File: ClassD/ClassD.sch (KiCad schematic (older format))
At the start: 37 parts, among them J1 RCJ-01X, J2 RCJ-01X, P1 CONN_01X02, SW1 FSM2JSMAA, U1 AP1117E50G-13, U2 TPA2008D2

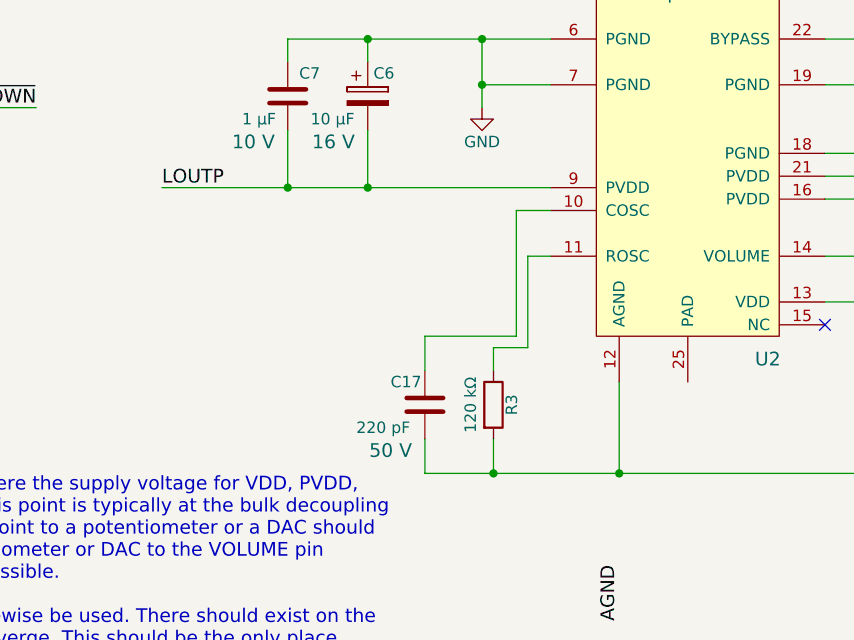
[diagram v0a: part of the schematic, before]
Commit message: Added the GND Zones and started routing
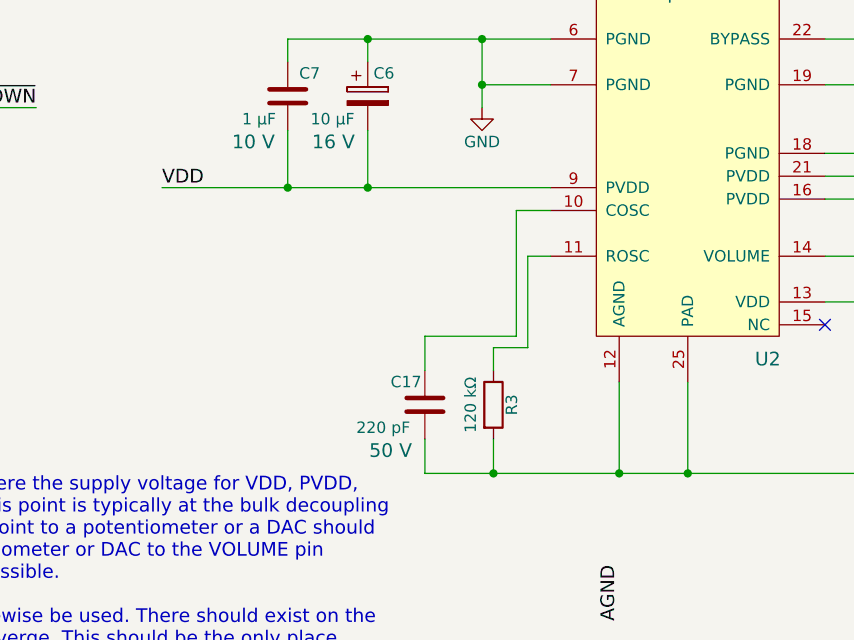
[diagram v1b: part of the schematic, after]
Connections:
- net GND: now also U2.25 (PAD)
- net LOUTP: no longer C6.2, C7.2, U2.9 (PVDD)
- net VDD: now also C6.2, C7.2, U2.9 (PVDD)
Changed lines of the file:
@@
 	3250 5200 4950 5200
 Text Label 3250 5200 0    60   ~ 0
-LOUTP
+VDD
 Text Label 6200 3850 0    60   ~ 0
 LOUTP
@@
 	5250 6050 5250 6450
 Connection ~ 5250 6450
+Wire Wire Line
+	5550 6050 5550 6450
+Connection ~ 5550 6450
 $EndSCHEMATC

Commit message: Wrapping up the routing
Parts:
- D1: footprint LEDs:LED_0805 -> LoudMouth-ClassD:LED_0805
- RV1: symbol POT -> POT-RESCUE-ClassD
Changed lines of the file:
@@
 EESchema Schematic File Version 2
+LIBS:ClassD-rescue
 LIBS:LoudMouth-ClassD
 LIBS:power
@@
 $EndComp
 $Comp
-L GND #PWR03
+L GND #PWR01
 U 1 1 56B60A69
 P 6650 6550
-F 0 "#PWR03" H 6650 6300 50  0001 C CNN
+F 0 "#PWR01" H 6650 6300 50  0001 C CNN
 F 1 "GND" H 6650 6400 50  0000 C CNN
 F 2 "" H 6650 6550 50  0000 C CNN
@@
 $EndComp
 $Comp
-L POT RV1
+L POT-RESCUE-ClassD RV1
 U 1 1 56B619ED
 P 7350 5850
@@
 ~SHUTDOWN
 $Comp
-L GND #PWR04
+L GND #PWR02
 U 1 1 56B6395C
 P 2200 6100
-F 0 "#PWR04" H 2200 5850 50  0001 C CNN
+F 0 "#PWR02" H 2200 5850 50  0001 C CNN
 F 1 "GND" H 2200 5950 50  0000 C CNN
 F 2 "" H 2200 6100 50  0000 C CNN
@@
 $EndComp
 $Comp
-L GND #PWR05
+L GND #PWR03
 U 1 1 56B66F4B
 P 7800 2300
-F 0 "#PWR05" H 7800 2050 50  0001 C CNN
+F 0 "#PWR03" H 7800 2050 50  0001 C CNN
 F 1 "GND" H 7800 2150 50  0000 C CNN
 F 2 "" H 7800 2300 50  0000 C CNN
@@
 $EndComp
 $Comp
-L GND #PWR06
+L GND #PWR04
 U 1 1 56B6779F
 P 8150 3800
-F 0 "#PWR06" H 8150 3550 50  0001 C CNN
+F 0 "#PWR04" H 8150 3550 50  0001 C CNN
 F 1 "GND" H 8150 3650 50  0000 C CNN
 F 2 "" H 8150 3800 50  0000 C CNN
@@
 $EndComp
 $Comp
-L GND #PWR07
+L GND #PWR05
 U 1 1 56B68F55
 P 8150 4450
-F 0 "#PWR07" H 8150 4200 50  0001 C CNN
+F 0 "#PWR05" H 8150 4200 50  0001 C CNN
 F 1 "GND" H 8150 4300 50  0000 C CNN
 F 2 "" H 8150 4450 50  0000 C CNN
@@
 $EndComp
 $Comp
-L GND #PWR08
+L GND #PWR06
 U 1 1 56B692A2
 P 7800 3000
-F 0 "#PWR08" H 7800 2750 50  0001 C CNN
+F 0 "#PWR06" H 7800 2750 50  0001 C CNN
 F 1 "GND" H 7800 2850 50  0000 C CNN
 F 2 "" H 7800 3000 50  0000 C CNN
@@
 	2450 1250 2450 1750
 $Comp
-L GND #PWR09
+L GND #PWR07
 U 1 1 56B7932F
 P 2450 1750
-F 0 "#PWR09" H 2450 1500 50  0001 C CNN
+F 0 "#PWR07" H 2450 1500 50  0001 C CNN
 F 1 "GND" H 2450 1600 50  0000 C CNN
 F 2 "" H 2450 1750 50  0000 C CNN
@@
 F 0 "D1" H 3800 1450 50  0000 C CNN
 F 1 "LED" H 3800 1250 50  0000 C CNN
-F 2 "LEDs:LED_0805" H 3800 1350 50  0001 C CNN
+F 2 "LoudMouth-ClassD:LED_0805" H 3800 1350 50  0001 C CNN
 F 3 "" H 3800 1350 50  0000 C CNN
 F 4 "Value" H 3800 1350 60  0001 C CNN "DigiKeyPN"
@@
 $EndComp
 $Comp
-L GND #PWR010
+L GND #PWR08
 U 1 1 5777C909
 P 3800 2050
-F 0 "#PWR010" H 3800 1800 50  0001 C CNN
+F 0 "#PWR08" H 3800 1800 50  0001 C CNN
 F 1 "GND" H 3800 1900 50  0000 C CNN
 F 2 "" H 3800 2050 50  0000 C CNN
@@
 Connection ~ 7700 6400
 $Comp
-L GND #PWR?
+L GND #PWR09
 U 1 1 57781854
 P 4650 4850
-F 0 "#PWR?" H 4650 4600 50  0001 C CNN
+F 0 "#PWR09" H 4650 4600 50  0001 C CNN
 F 1 "GND" H 4650 4700 50  0000 C CNN
 F 2 "" H 4650 4850 50  0000 C CNN
@@
 	7650 4750 7650 4550
 $Comp
-L GND #PWR?
+L GND #PWR010
 U 1 1 577837B4
 P 6900 4900
-F 0 "#PWR?" H 6900 4650 50  0001 C CNN
+F 0 "#PWR010" H 6900 4650 50  0001 C CNN
 F 1 "GND" H 6900 4750 50  0000 C CNN
 F 2 "" H 6900 4900 50  0000 C CNN

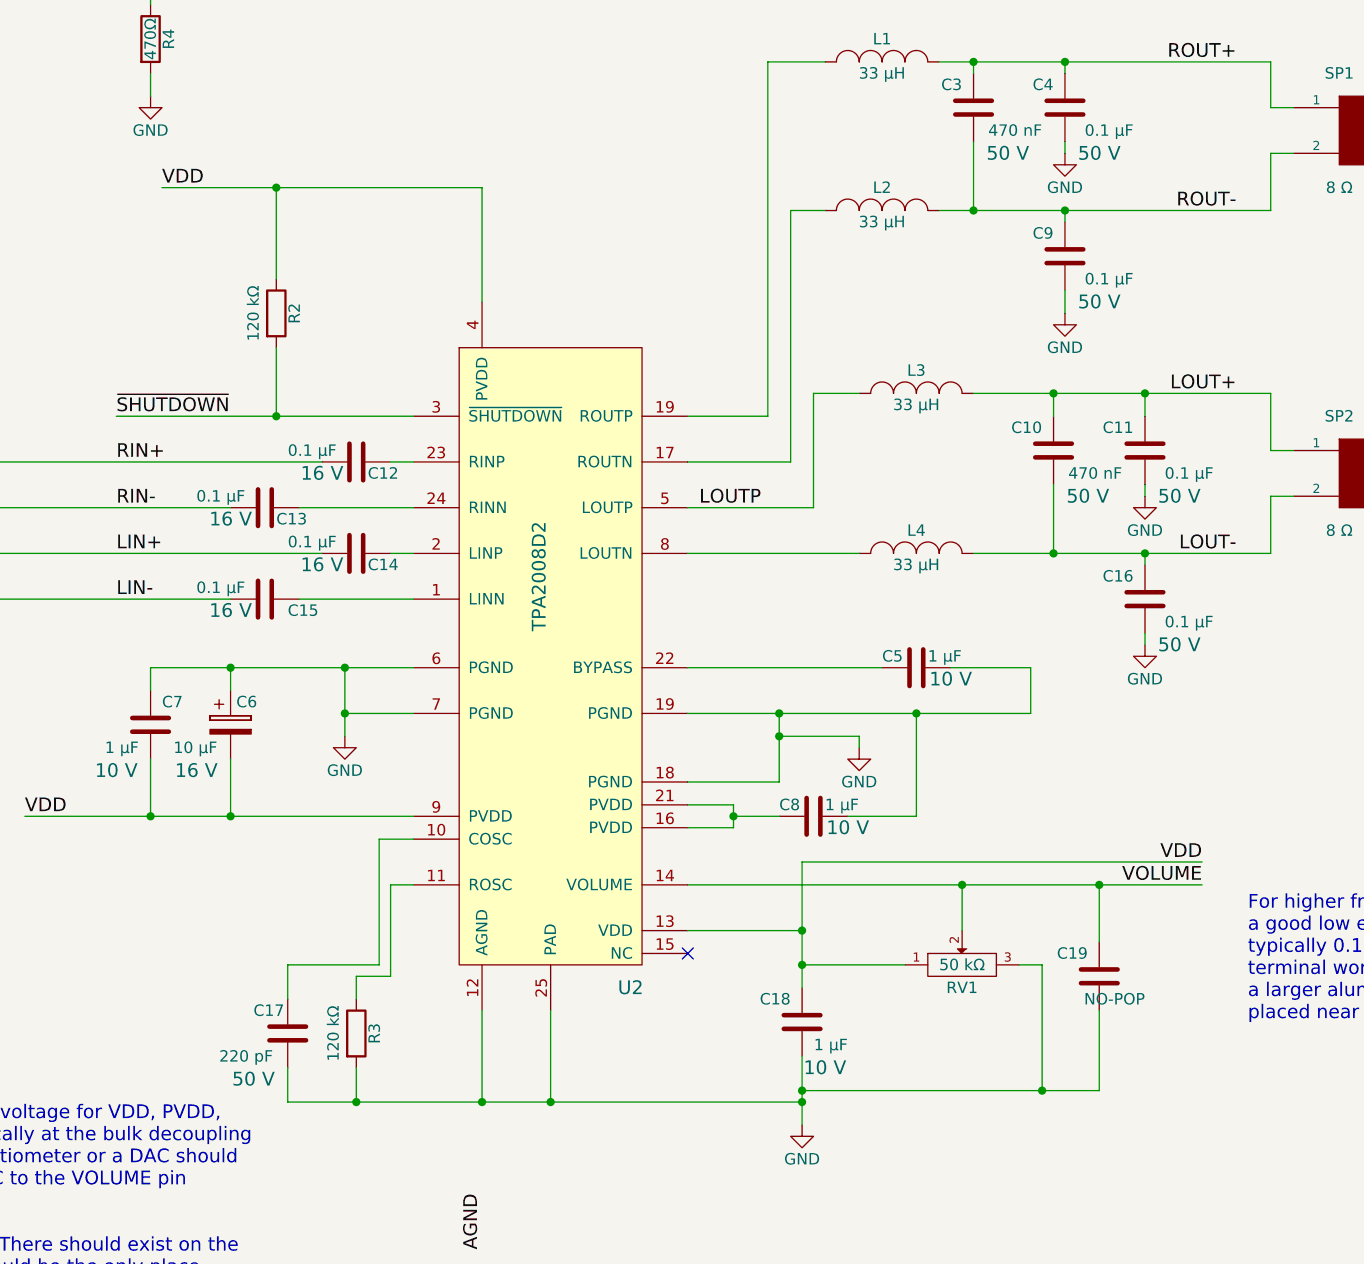
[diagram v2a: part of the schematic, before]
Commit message: Updated the layout with some circuit changes as well as the audio chip footprint.
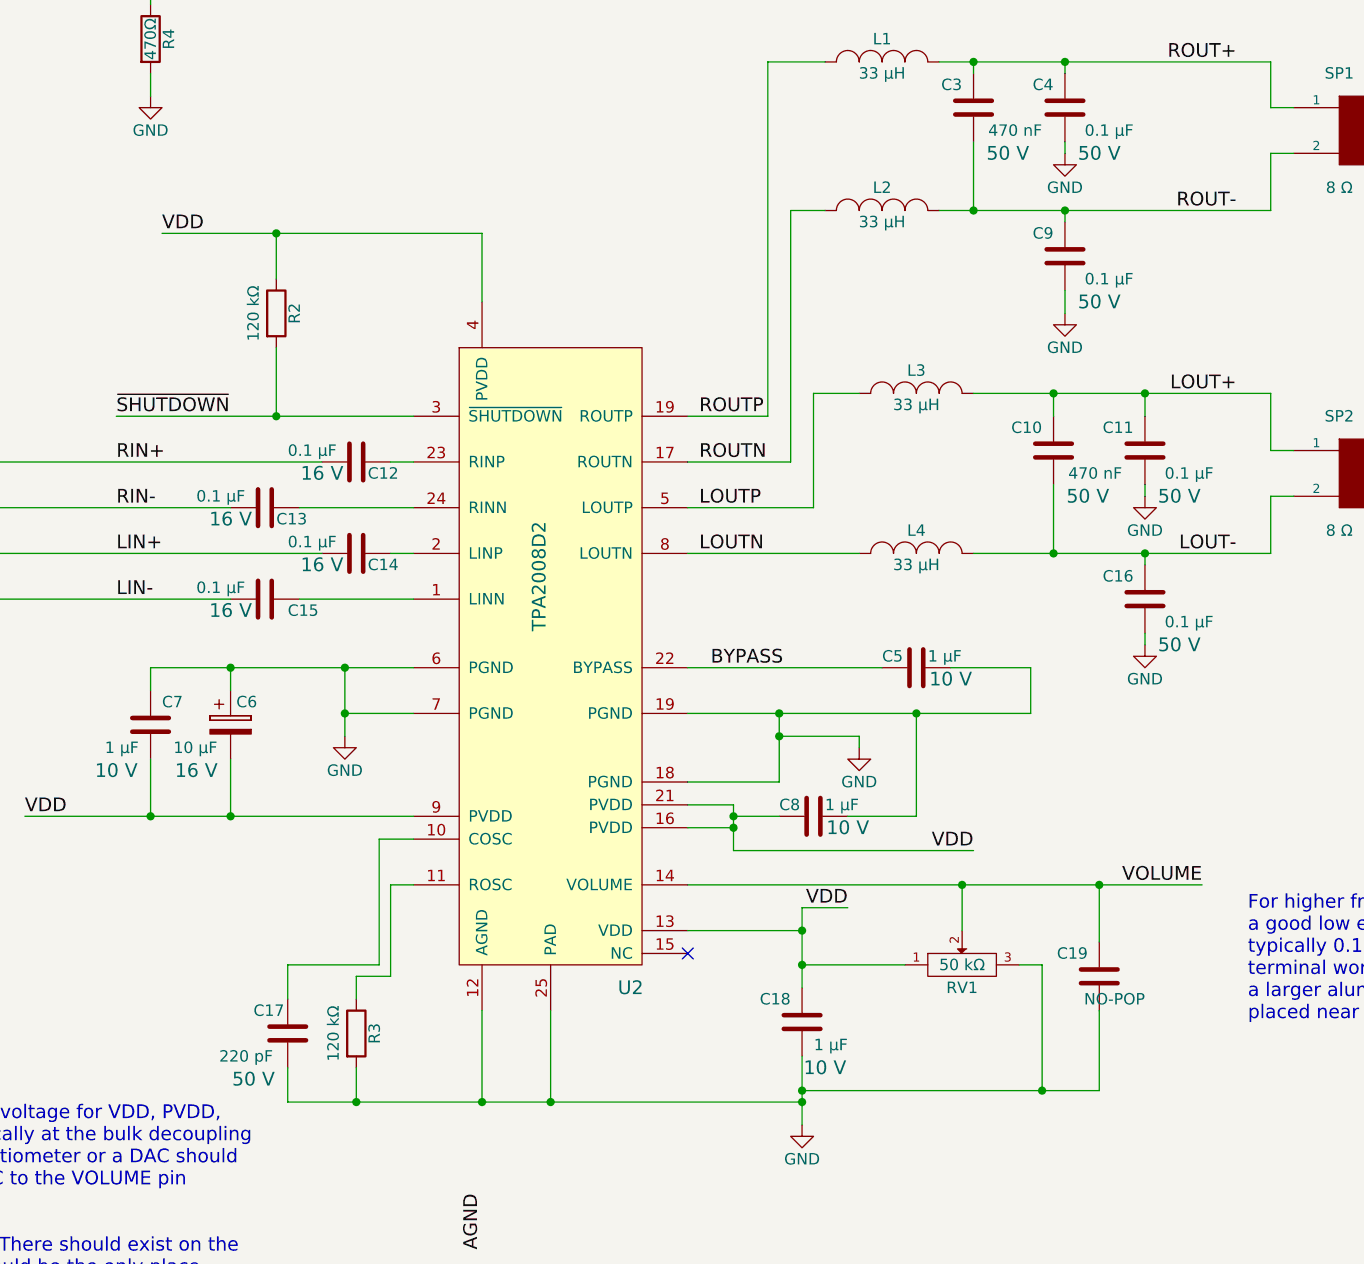
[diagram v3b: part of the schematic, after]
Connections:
- net VDD: now also C8.2, U2.16 (PVDD), U2.21 (PVDD)
- net ROUTN: now reaches L2.1, U2.17 (ROUTN)
- net ROUTP: now reaches L1.1, U2.19 (ROUTP)
- net BYPASS: now reaches C5.2, U2.22 (BYPASS)
- net LOUTN: now reaches L4.1, U2.8 (LOUTN)
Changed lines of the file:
@@
 LIN-
 NoConn ~ 6150 5800
-Text Label 3850 2450 0    60   ~ 0
+Text Label 3850 2650 0    60   ~ 0
 VDD
 $Comp
@@
 	1    0    0    -1
 $EndComp
-Text Label 8400 5400 2    60   ~ 0
+Text Label 6850 5600 2    60   ~ 0
 VDD
 $Comp
@@
 	6600 3650 6150 3650
 Wire Wire Line
-	5250 2450 5250 2950
-Wire Wire Line
-	4400 6450 6650 6450
+	5250 2650 5250 2950
+Wire Wire Line
+	6650 6450 4400 6450
 Wire Wire Line
 	4700 6300 4700 6450
@@
 	6650 6250 6650 6550
 Wire Wire Line
-	6650 5400 6650 5950
+	6650 5600 6650 5950
 Wire Wire Line
 	6650 6400 7950 6400
@@
 	3650 3450 4950 3450
 Wire Wire Line
-	4350 2450 4350 2850
+	4350 2650 4350 2850
 Wire Wire Line
 	4350 3150 4350 3450
@@
 AGND
 Wire Wire Line
-	8400 5400 6650 5400
-Wire Wire Line
 	7100 5850 6650 5850
 Connection ~ 6650 5850
@@
 	7650 4550 7300 4550
 Wire Wire Line
-	6150 5250 6350 5250
-Wire Wire Line
-	6350 5250 6350 5150
+	6350 5250 6150 5250
+Wire Wire Line
+	6350 5150 6350 5350
 Wire Wire Line
 	6350 5150 6150 5150
@@
 	6550 5200 6350 5200
 Wire Wire Line
-	6150 5050 6550 5050
-Wire Wire Line
-	6550 5050 6550 4750
+	6550 5050 6150 5050
+Wire Wire Line
+	6550 4750 6550 5050
 Connection ~ 6550 4750
 Wire Wire Line
@@
 Connection ~ 6550 4850
 Wire Wire Line
-	3850 2450 5250 2450
-Connection ~ 4350 2450
+	3850 2650 5250 2650
+Connection ~ 4350 2650
 Connection ~ 4700 6450
 Wire Wire Line
@@
 	5550 6050 5550 6450
 Connection ~ 5550 6450
+Connection ~ 6350 5250
+Text Label 7400 5350 2    60   ~ 0
+VDD
+Text Label 6200 4050 0    60   ~ 0
+LOUTN
+Text Label 6200 3450 0    60   ~ 0
+ROUTP
+Text Label 6200 3650 0    60   ~ 0
+ROUTN
+Text Label 6250 4550 0    60   ~ 0
+BYPASS
+Wire Wire Line
+	6650 5600 6850 5600
+Wire Wire Line
+	6350 5350 7400 5350
 $EndSCHEMATC
